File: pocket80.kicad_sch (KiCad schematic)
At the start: 0 parts

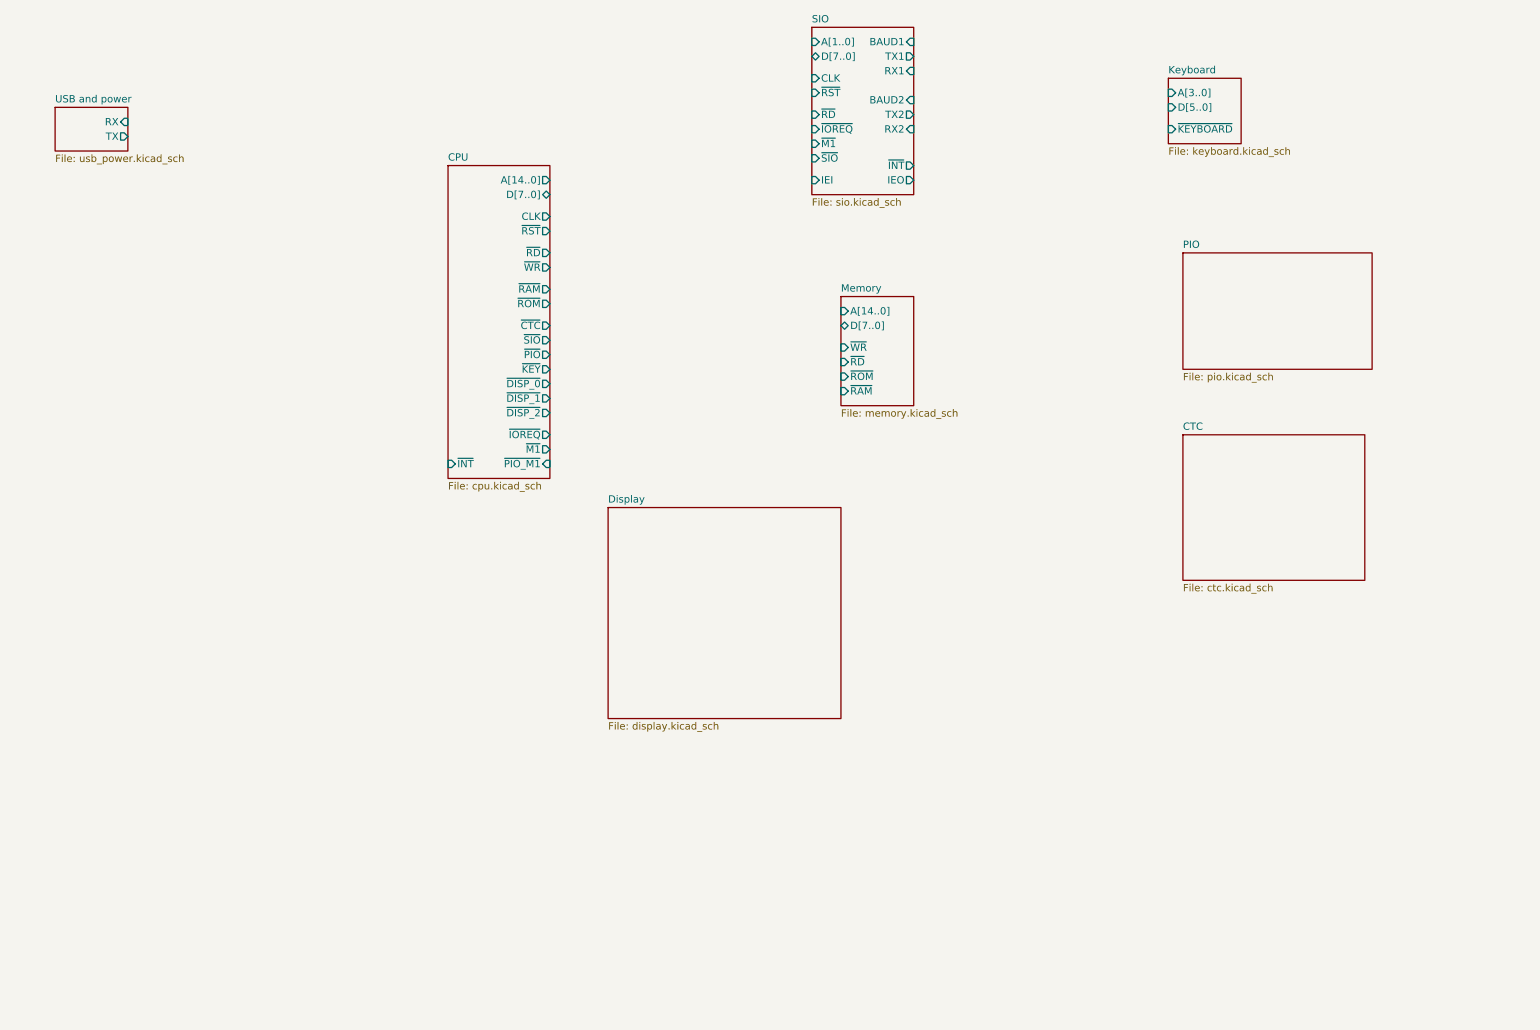
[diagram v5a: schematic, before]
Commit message: HW: Finish CTC sound generator
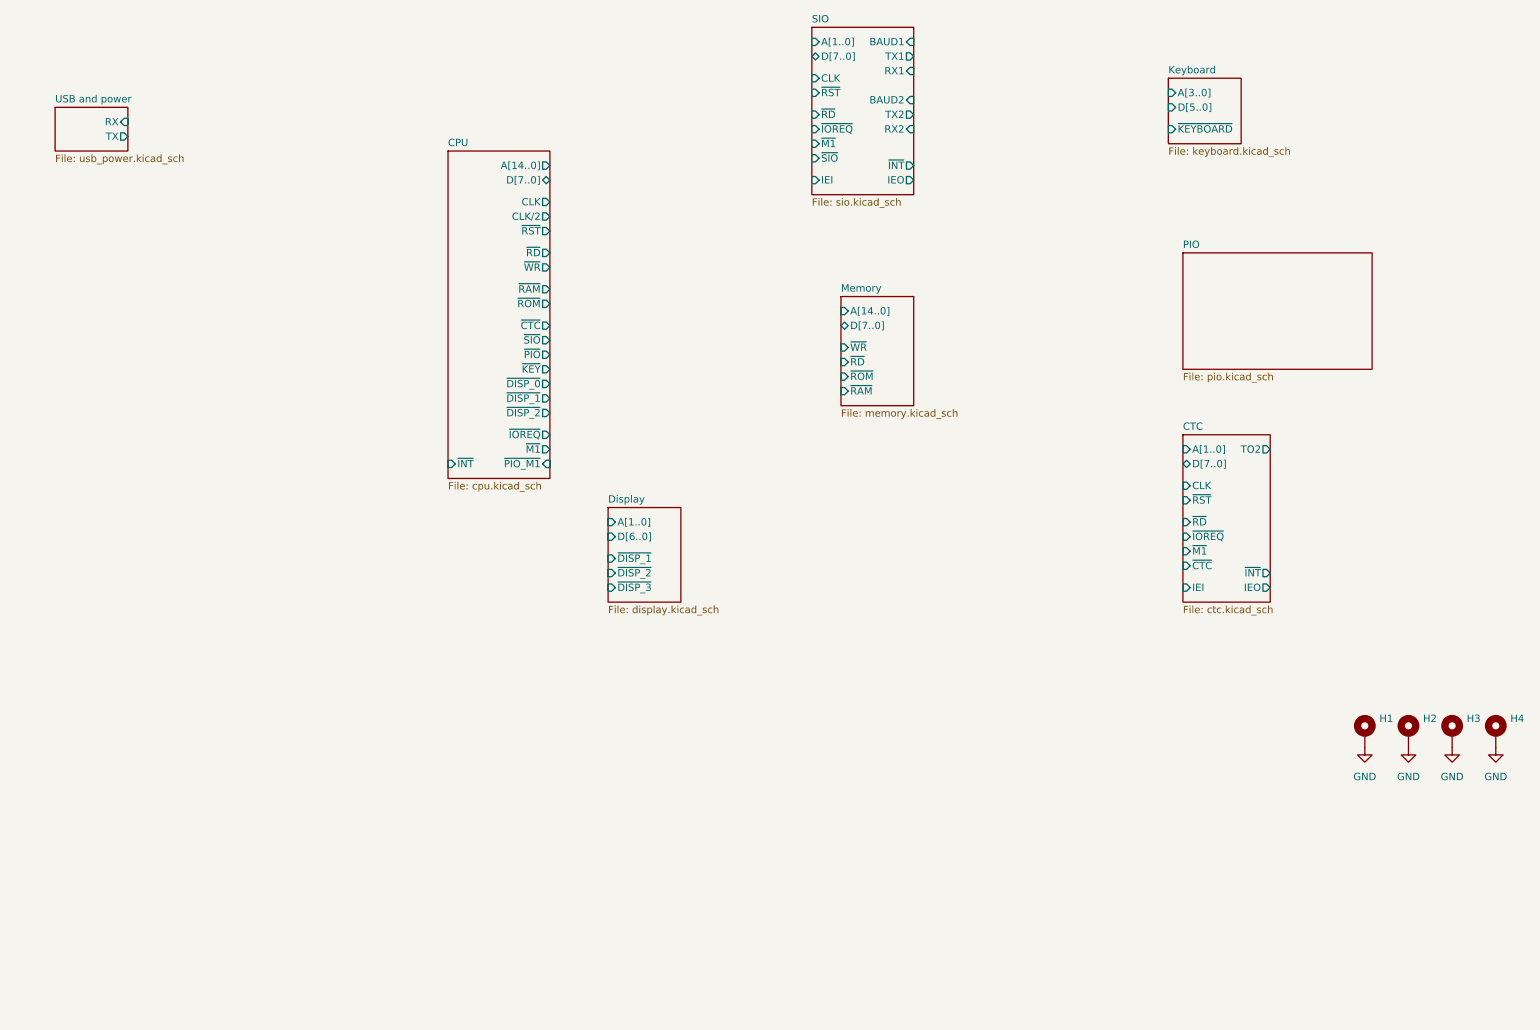
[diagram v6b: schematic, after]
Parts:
- added H1, H2, H3, H4: MountingHole_Pad_MP, MountingHole:MountingHole_3.2mm_M3_Pad_Via, symbol Mechanical:MountingHole_Pad_MP
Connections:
- new net GND: H1.MP, H2.MP, H3.MP, H4.MP
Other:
- sheet CPU ports: added CLK/2; removed none
- sheet CTC ports: added A[1..0], CLK, D[7..0], IEI, IEO, TO2, ~{CTC}, ~{INT}, ~{IOREQ}, ~{M1}, ~{RD}, ~{RST}; removed none
- sheet Display ports: added A[1..0], D[6..0], ~{DISP_1}, ~{DISP_2}, ~{DISP_3}; removed none

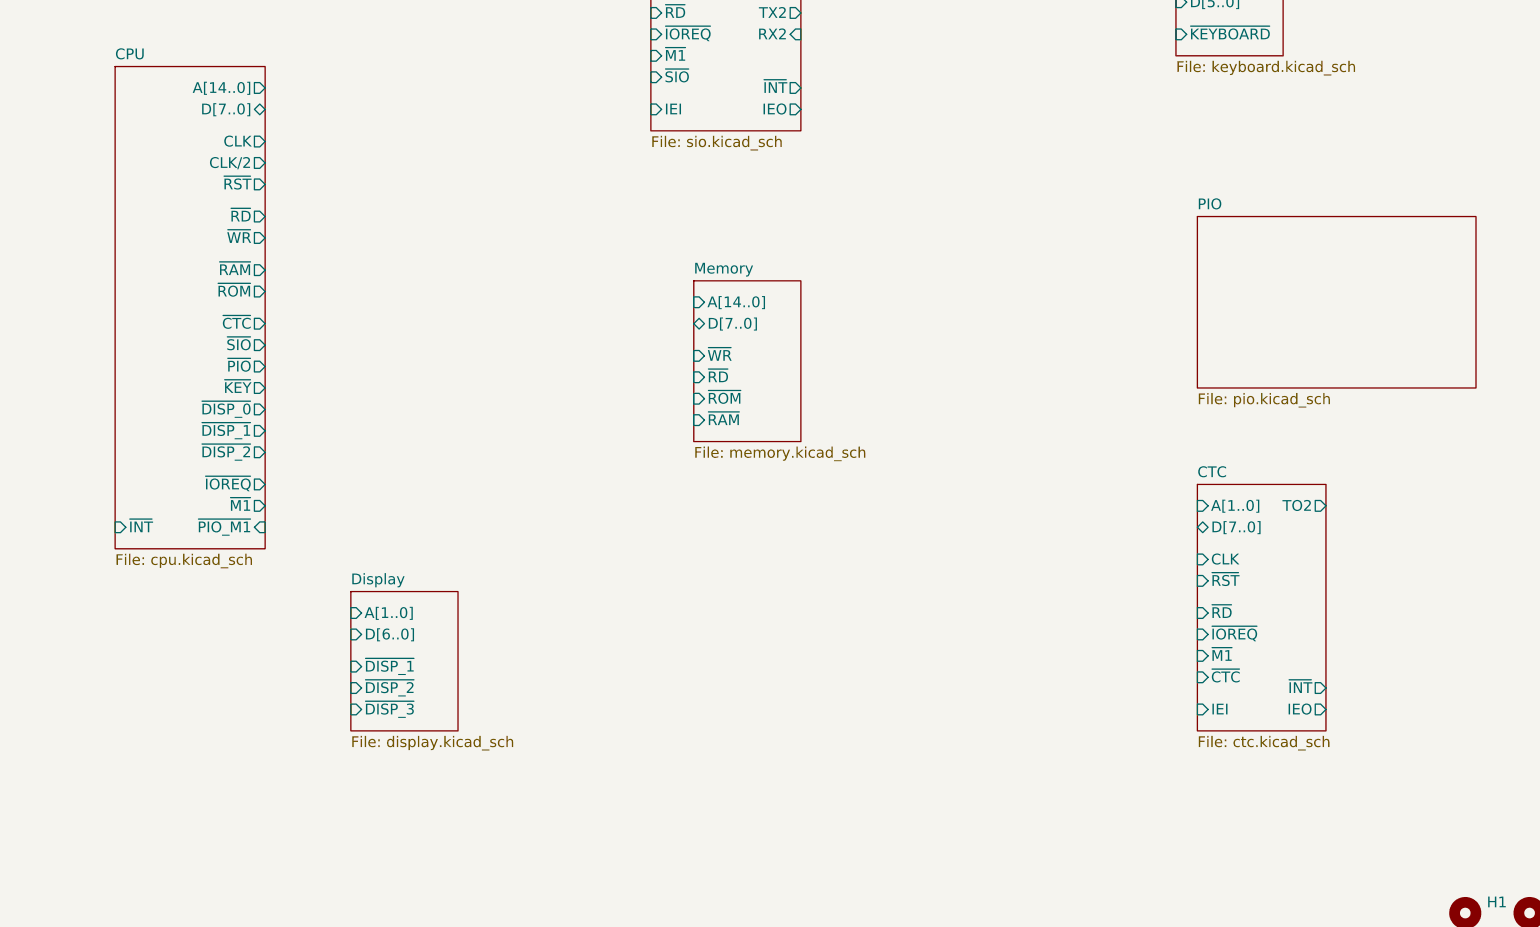
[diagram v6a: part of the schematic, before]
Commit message: HW: Add rst button, sync pins
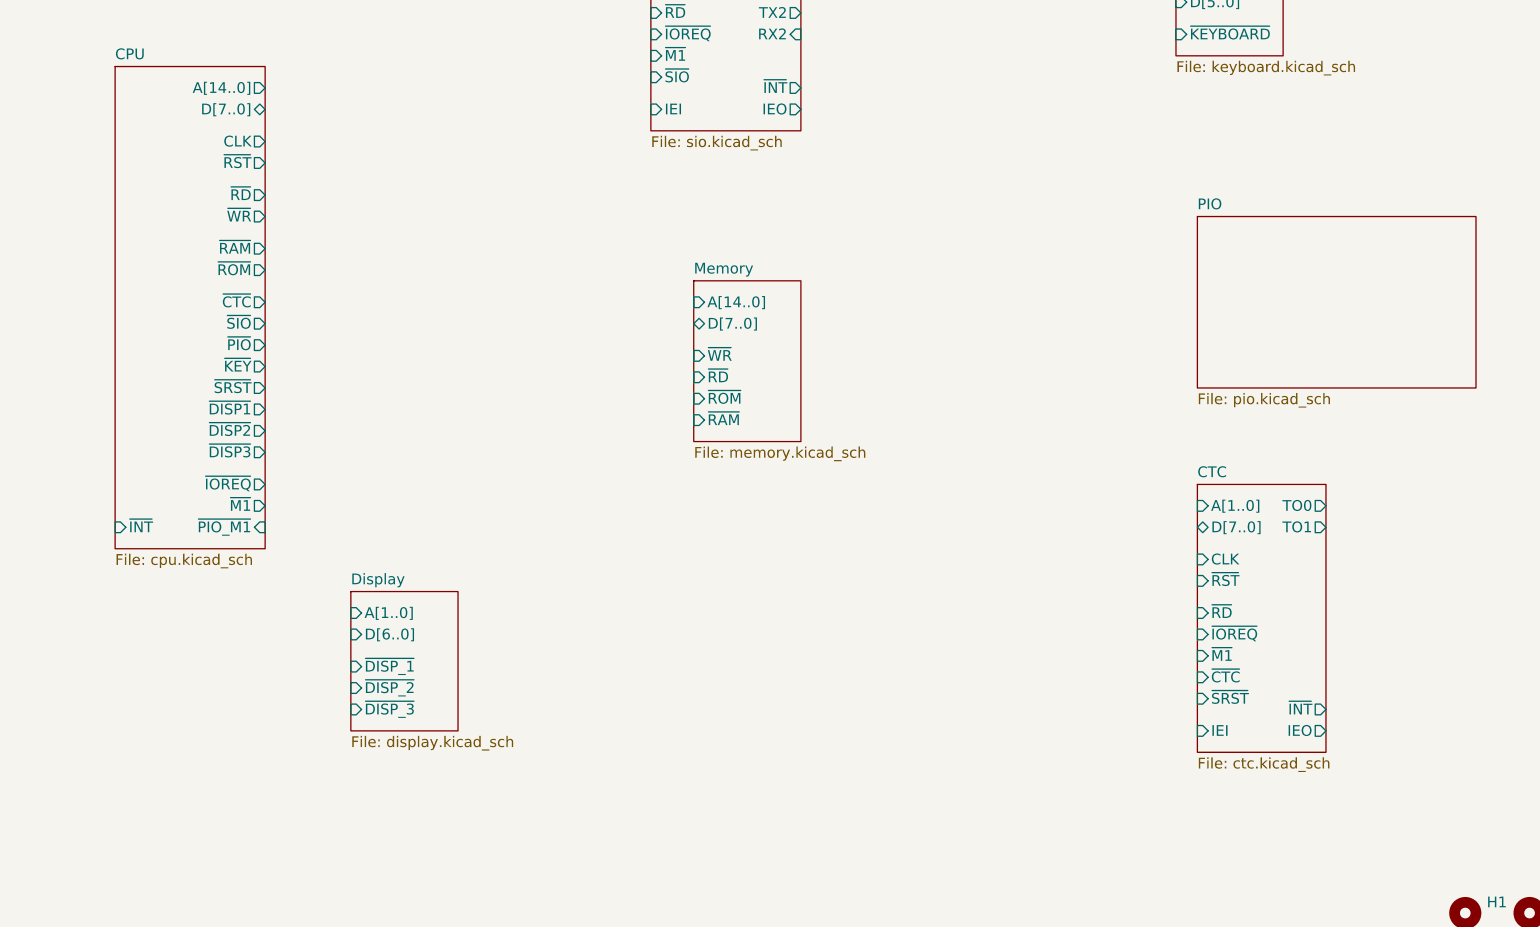
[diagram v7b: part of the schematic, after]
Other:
- sheet CPU ports: added ~{DISP1}, ~{DISP2}, ~{DISP3}, ~{SRST}; removed CLK/2, ~{DISP_0}, ~{DISP_1}, ~{DISP_2}
- sheet CTC ports: added TO0, TO1, ~{SRST}; removed TO2
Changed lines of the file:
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@@
 	(sheet
 		(at 222.25 102.87)
-		(size 15.24 29.21)
+		(size 15.24 31.75)
 		(exclude_from_sim no)
 		(in_bom yes)
@@
 		)
 		(property "Sheetfile" "ctc.kicad_sch"
-			(at 222.25 132.6646 0)
+			(at 222.25 135.2046 0)
 			(effects
 				(font
@@
 		)
 		(pin "IEI" input
-			(at 222.25 129.54 180)
+			(at 222.25 132.08 180)
 			(effects
 				(font
@@
 		)
 		(pin "IEO" output
-			(at 237.49 129.54 0)
-			(effects
-				(font
-					(size 1.27 1.27)
-				)
-				(justify right)
-			)
-		)
-		(pin "TO2" output
-			(at 237.49 105.41 0)
+			(at 237.49 132.08 0)
 			(effects
 				(font
@@
 		)
 		(pin "~{INT}" output
-			(at 237.49 127 0)
+			(at 237.49 129.54 0)
 			(effects
 				(font
@@
 		(pin "~{RST}" input
 			(at 222.25 114.3 180)
+			(effects
+				(font
+					(size 1.27 1.27)
+				)
+				(justify left)
+			)
+		)
+		(pin "TO0" output
+			(at 237.49 105.41 0)
+			(effects
+				(font
+					(size 1.27 1.27)
+				)
+				(justify right)
+			)
+		)
+		(pin "TO1" output
+			(at 237.49 107.95 0)
+			(effects
+				(font
+					(size 1.27 1.27)
+				)
+				(justify right)
+			)
+		)
+		(pin "~{SRST}" input
+			(at 222.25 128.27 180)
 			(effects
 				(font
@@
 		)
 		(pin "~{CTC}" output
-			(at 111.76 83.82 0)
+			(at 111.76 81.28 0)
 			(effects
 				(font
@@
 		)
 		(pin "~{KEY}" output
-			(at 111.76 91.44 0)
+			(at 111.76 88.9 0)
 			(effects
 				(font
@@
 		)
 		(pin "~{PIO}" output
-			(at 111.76 88.9 0)
+			(at 111.76 86.36 0)
 			(effects
 				(font
@@
 		)
 		(pin "~{RAM}" output
+			(at 111.76 74.93 0)
+			(effects
+				(font
+					(size 1.27 1.27)
+				)
+				(justify right)
+			)
+		)
+		(pin "~{RD}" output
+			(at 111.76 68.58 0)
+			(effects
+				(font
+					(size 1.27 1.27)
+				)
+				(justify right)
+			)
+		)
+		(pin "~{ROM}" output
 			(at 111.76 77.47 0)
 			(effects
@@
 			)
 		)
-		(pin "~{RD}" output
+		(pin "~{RST}" output
+			(at 111.76 64.77 0)
+			(effects
+				(font
+					(size 1.27 1.27)
+				)
+				(justify right)
+			)
+		)
+		(pin "~{SIO}" output
+			(at 111.76 83.82 0)
+			(effects
+				(font
+					(size 1.27 1.27)
+				)
+				(justify right)
+			)
+		)
+		(pin "~{WR}" output
 			(at 111.76 71.12 0)
-			(effects
-				(font
-					(size 1.27 1.27)
-				)
-				(justify right)
-			)
-		)
-		(pin "~{ROM}" output
-			(at 111.76 80.01 0)
-			(effects
-				(font
-					(size 1.27 1.27)
-				)
-				(justify right)
-			)
-		)
-		(pin "~{RST}" output
-			(at 111.76 67.31 0)
-			(effects
-				(font
-					(size 1.27 1.27)
-				)
-				(justify right)
-			)
-		)
-		(pin "~{SIO}" output
-			(at 111.76 86.36 0)
-			(effects
-				(font
-					(size 1.27 1.27)
-				)
-				(justify right)
-			)
-		)
-		(pin "~{WR}" output
-			(at 111.76 73.66 0)
-			(effects
-				(font
-					(size 1.27 1.27)
-				)
-				(justify right)
-			)
-		)
-		(pin "~{DISP_0}" output
-			(at 111.76 93.98 0)
-			(effects
-				(font
-					(size 1.27 1.27)
-				)
-				(justify right)
-			)
-		)
-		(pin "~{DISP_1}" output
-			(at 111.76 96.52 0)
-			(effects
-				(font
-					(size 1.27 1.27)
-				)
-				(justify right)
-			)
-		)
-		(pin "~{DISP_2}" output
-			(at 111.76 99.06 0)
 			(effects
 				(font
@@
 			)
 		)
-		(pin "CLK{slash}2" output
-			(at 111.76 64.77 0)
-			(effects
-				(font
+		(pin "~{SRST}" output
+			(at 111.76 91.44 0)
+			(effects
+				(font
+					(size 1.27 1.27)
+				)
+				(justify right)
+			)
+		)
+		(pin "~{DISP1}" output
+			(at 111.76 93.98 0)
+			(effects
+				(font
+					(size 1.27 1.27)
+				)
+				(justify right)
+			)
+		)
+		(pin "~{DISP2}" output
+			(at 111.76 96.52 0)
+			(effects
+				(font
+					(size 1.27 1.27)
+				)
+				(justify right)
+			)
+		)
+		(pin "~{DISP3}" output
+			(at 111.76 99.06 0)
+			(effects
+				(font

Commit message: HW: PIO done
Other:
- added sheet Expansion (expansion.kicad_sch)
- sheet PIO ports: added ARDY, A[1..0], CLK, D[7..0], IEI, IEO, PORTA[7..0], PORTB[1..0], ~{ASTB}, ~{INT}, ~{IOREQ}, ~{M1}, ~{PIO}, ~{RD}; removed none
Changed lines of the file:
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@@
 	(paper "A4")
 	(title_block
-		(date "2025-10-14")
+		(date "2025-10-16")
 		(rev "A")
 		(company "A.K.")
@@
 	)
 	(sheet
-		(at 222.25 71.12)
-		(size 33.02 20.32)
+		(at 222.25 60.96)
+		(size 22.86 26.67)
 		(exclude_from_sim no)
 		(in_bom yes)
@@
 		)
 		(property "Sheetname" "PIO"
-			(at 222.25 70.4084 0)
+			(at 222.25 60.2484 0)
 			(effects
 				(font
@@
 		)
 		(property "Sheetfile" "pio.kicad_sch"
-			(at 222.25 92.0246 0)
+			(at 222.25 88.2146 0)
 			(effects
 				(font
@@
 				)
 				(justify left top)
+			)
+		)
+		(pin "ARDY" output
+			(at 245.11 66.04 0)
+			(effects
+				(font
+					(size 1.27 1.27)
+				)
+				(justify right)
+			)
+		)
+		(pin "A[1..0]" input
+			(at 222.25 63.5 180)
+			(effects
+				(font
+					(size 1.27 1.27)
+				)
+				(justify left)
+			)
+		)
+		(pin "CLK" input
+			(at 222.25 69.85 180)
+			(effects
+				(font
+					(size 1.27 1.27)
+				)
+				(justify left)
+			)
+		)
+		(pin "D[7..0]" bidirectional
+			(at 222.25 66.04 180)
+			(effects
+				(font
+					(size 1.27 1.27)
+				)
+				(justify left)
+			)
+		)
+		(pin "IEI" input
+			(at 222.25 85.09 180)
+			(effects
+				(font
+					(size 1.27 1.27)
+				)
+				(justify left)
+			)
+		)
+		(pin "IEO" output
+			(at 245.11 85.09 0)
+			(effects
+				(font
+					(size 1.27 1.27)
+				)
+				(justify right)
+			)
+		)
+		(pin "PORTA[7..0]" bidirectional
+			(at 245.11 63.5 0)
+			(effects
+				(font
+					(size 1.27 1.27)
+				)
+				(justify right)
+			)
+		)
+		(pin "PORTB[1..0]" bidirectional
+			(at 245.11 72.39 0)
+			(effects
+				(font
+					(size 1.27 1.27)
+				)
+				(justify right)
+			)
+		)
+		(pin "~{ASTB}" input
+			(at 245.11 68.58 0)
+			(effects
+				(font
+					(size 1.27 1.27)
+				)
+				(justify right)
+			)
+		)
+		(pin "~{INT}" output
+			(at 245.11 82.55 0)
+			(effects
+				(font
+					(size 1.27 1.27)
+				)
+				(justify right)
+			)
+		)
+		(pin "~{IOREQ}" input
+			(at 222.25 76.2 180)
+			(effects
+				(font
+					(size 1.27 1.27)
+				)
+				(justify left)
+			)
+		)
+		(pin "~{M1}" input
+			(at 222.25 78.74 180)
+			(effects
+				(font
+					(size 1.27 1.27)
+				)
+				(justify left)
+			)
+		)
+		(pin "~{PIO}" input
+			(at 222.25 81.28 180)
+			(effects
+				(font
+					(size 1.27 1.27)
+				)
+				(justify left)
+			)
+		)
+		(pin "~{RD}" input
+			(at 222.25 73.66 180)
+			(effects
+				(font
+					(size 1.27 1.27)
+				)
+				(justify left)
 			)
 		)
@@
 				)
 			)
+		)
+	)
+	(sheet
+		(at 165.1 111.76)
+		(size 19.05 13.97)
+		(exclude_from_sim no)
+		(in_bom yes)
+		(on_board yes)
+		(dnp no)
+		(fields_autoplaced yes)
+		(stroke
+			(width 0.1524)
+			(type solid)
+		)
+		(fill
+			(color 0 0 0 0.0000)
+		)
+		(property "Sheetname" "Expansion"
+			(at 165.1 111.0484 0)
+			(effects
+				(font
+					(size 1.27 1.27)
+				)
+				(justify left bottom)
+			)
+		)
+		(property "Sheetfile" "expansion.kicad_sch"
+			(at 165.1 126.3146 0)
+			(effects
+				(font
+					(size 1.27 1.27)
+				)
+				(justify left top)
+			)
+		)
+		(pin "ARDY" input
+			(at 165.1 116.84 180)
+			(effects
+				(font
+					(size 1.27 1.27)
+				)
+				(justify left)
+			)
+		)
+		(pin "PORTA[7..0]" bidirectional
+			(at 165.1 114.3 180)
+			(effects
+				(font
+					(size 1.27 1.27)
+				)
+				(justify left)
+			)
+		)
+		(pin "PORTB[1..0]" bidirectional
+			(at 165.1 123.19 180)
+			(effects
+				(font
+					(size 1.27 1.27)
+				)
+				(justify left)
+			)
+		)
+		(pin "RX" output
+			(at 184.15 114.3 0)
+			(effects
+				(font
+					(size 1.27 1.27)
+				)
+				(justify right)
+			)
+		)
+		(pin "TX" input
+			(at 184.15 116.84 0)
+			(effects
+				(font
+					(size 1.27 1.27)
+				)
+				(justify right)
+			)
+		)
+		(pin "ZC{slash}TO0" input
+			(at 184.15 120.65 0)
+			(effects
+				(font
+					(size 1.27 1.27)
+				)
+				(justify right)
+			)
+		)
+		(pin "~{ASTB}" output
+			(at 165.1 119.38 180)
+			(effects
+				(font
+					(size 1.27 1.27)
+				)
+				(justify left)
+			)
+		)
+		(instances
+			(project "pocket80"
+				(path "/328c075d-c706-4d2d-bd37-a88a0c604482"
+					(page "10")
+				)
+			)
